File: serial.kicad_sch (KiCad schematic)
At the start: 28 parts, among them U12 6551, U13 4069, U14 LM348DR, X2 1.8432MHz

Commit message: fix OE timing on SRAM
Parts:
- renumbered D2 to D10, D2 to D11, D2 to D12, D2 to D13, D2 to D14, D2 to D15, D2 to D16, D2 to D17, R28 to R35, R28 to R37, R28 to R44, R28 to R53, R28 to R54, R28 to R55, R28 to R57, R28 to R58, R28 to R59, R28 to R60

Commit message: update page info
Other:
- company: (none) -> Dragon Data
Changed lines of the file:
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@@
 (kicad_sch (version 20230121) (generator eeschema)
-  (paper "A4")
+  (paper "A3")
+  (title_block
+    (date "2024-01-07")
+    (rev "3.0")
+    (company "Dragon Data")
+    (comment 1 "Modified by Julian Brown")
+    (comment 2 "SAMx4 by Ciaran Anscomb")
+  )
   (junction (at 226.06 24.13) (diameter 0) (color 0 0 0 0)
   )

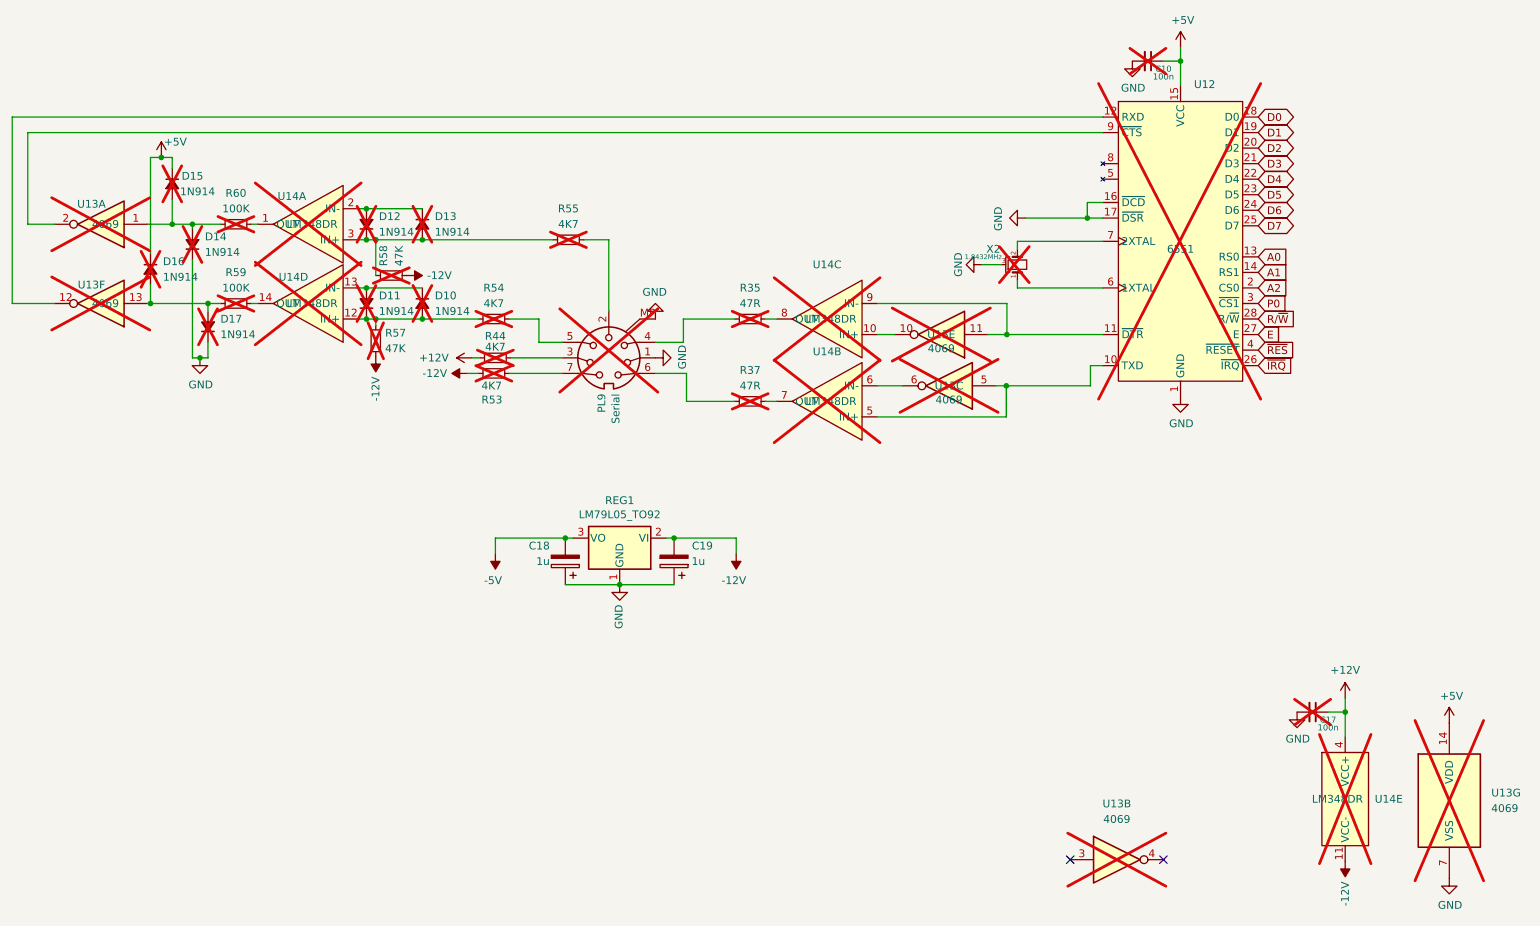
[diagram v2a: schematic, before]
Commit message: switch to fpga
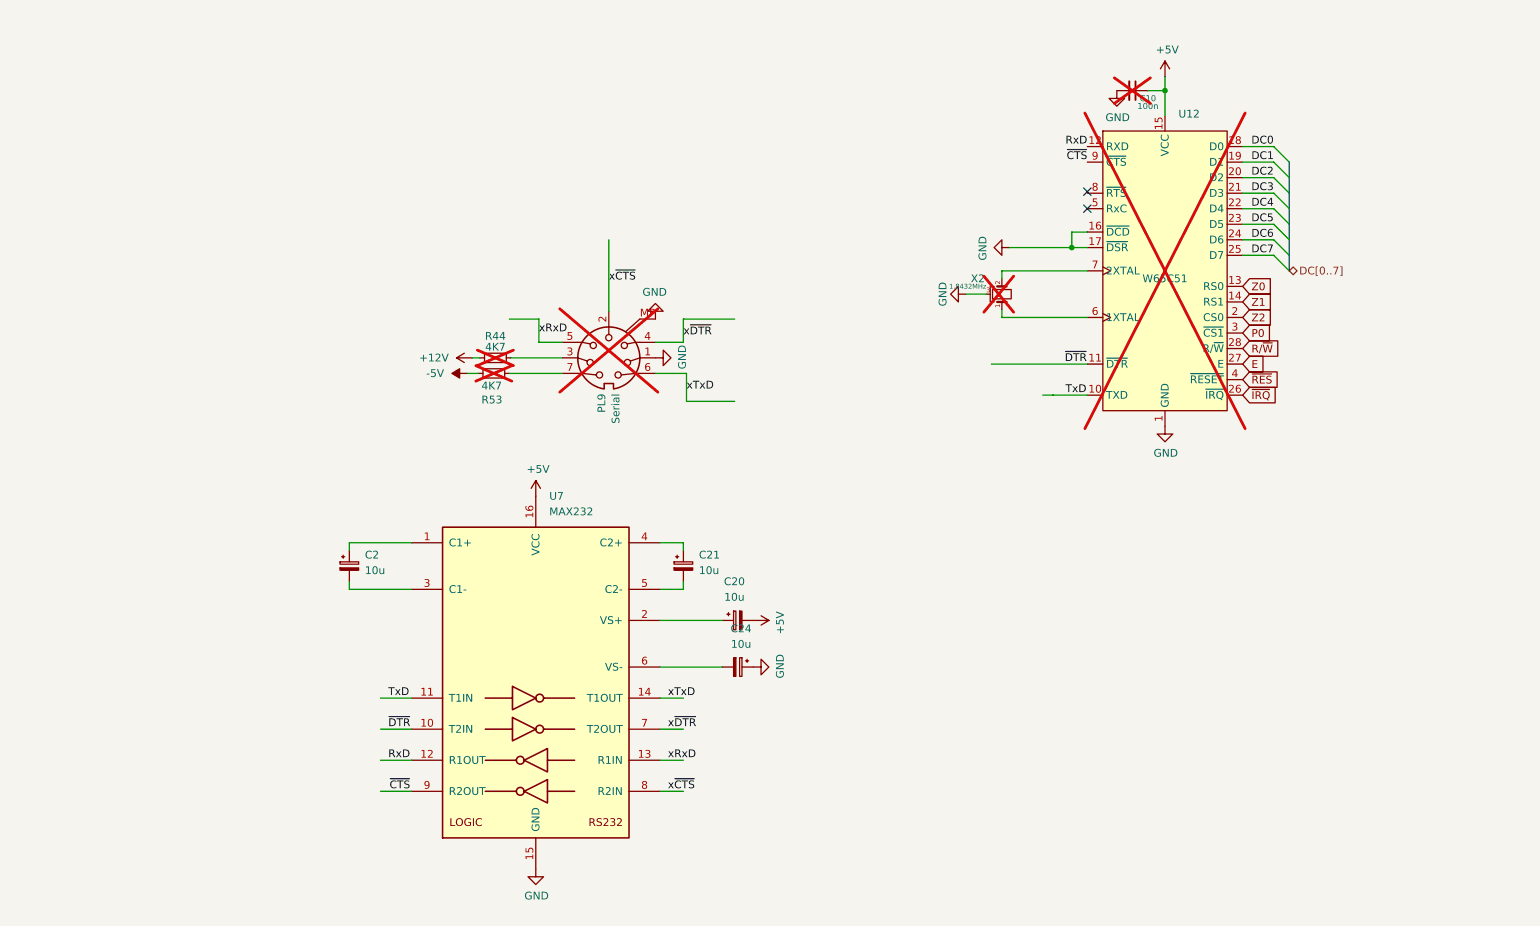
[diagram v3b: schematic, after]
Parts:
- removed C17: 100n, Capacitor_SMD:C_0805_2012Metric_Pad1.18x1.45mm_HandSolder, symbol Device:C_Small
- removed C18, C19: 1u, Capacitor_Tantalum_SMD:CP_EIA-3216-18_Kemet-A_Pad1.58x1.35mm_HandSolder, symbol Device:C_Polarized
- removed D10, D11, D12, D13, D14, D15, D16, D17: 1N914, Diode_SMD:D_SOD-323_HandSoldering, symbol Device:D_Small_Filled
- removed R35, R37: 47R, Resistor_SMD:R_0805_2012Metric_Pad1.20x1.40mm_HandSolder, symbol Device:R_Small
- removed R54, R55: 4K7, Resistor_SMD:R_0805_2012Metric_Pad1.20x1.40mm_HandSolder, symbol Device:R_Small
- removed R57, R58: 47K, Resistor_SMD:R_0805_2012Metric_Pad1.20x1.40mm_HandSolder, symbol Device:R_Small
- removed R59, R60: 100K, Resistor_SMD:R_0805_2012Metric_Pad1.20x1.40mm_HandSolder, symbol Device:R_Small
- removed REG1: LM79L05_TO92, Package_TO_SOT_SMD:SOT-89-3_Handsoldering, symbol Regulator_Linear:LM79L05_TO92
- removed U13: 4069, Package_SO:SOIC-14_3.9x8.7mm_P1.27mm, symbol 4xxx:4069
- removed U14: LM348DR, Package_SO:SOIC-14_3.9x8.7mm_P1.27mm, symbol Motorola PIA:LM348x
- added C2, C20, C21, C24: 10u, Capacitor_SMD:CP_Elec_5x5.3, symbol Device:C_Polarized_Small
- added U7: MAX232, Package_SO:SOIC-16_3.9x9.9mm_P1.27mm, symbol Interface_UART:MAX232
- U12: value 6551 -> W65C51; footprint Package_DIP:DIP-28_W15.24mm -> Package_LCC:PLCC-28_SMD-Socket
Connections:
- net -12V is gone; now on net -5V: R53.2
- net +5V: now also C20.2, U7.16 (VCC)
- net GND: now also C24.1, U7.15 (GND)
- net TxD: now reaches U12.10 (TXD)
- net TxD: now also U7.11 (T1IN)
- net xRxD: now reaches PL9.5
- net xRxD: now also U7.13 (R1IN)
- net ~{DTR}: now reaches U12.11 (~{DTR})
- net ~{DTR}: now also U7.10 (T2IN)
- net RxD: now reaches U12.12 (RXD)
- net RxD: now also U7.12 (R1OUT)
- net ~{CTS}: now reaches U12.9 (~{CTS})
- net ~{CTS}: now also U7.9 (R2OUT)
- net xTxD: now reaches PL9.6
- net xTxD: now also U7.14 (T1OUT)
- net x~{DTR}: now reaches PL9.4
- net x~{DTR}: now also U7.7 (T2OUT)
- net x~{CTS}: now reaches PL9.2
- net x~{CTS}: now also U7.8 (R2IN)
- net A0 renamed Z0
- net A1 renamed Z1
- net A2 renamed Z2
- net D0 renamed DC0
- net D1 renamed DC1
- net D2 renamed DC2
- net D3 renamed DC3
- net D4 renamed DC4
- net D5 renamed DC5
- net D6 renamed DC6
- net D7 renamed DC7
- new net: C20.1, U7.2 (VS+)
- new net: C2.1, U7.1 (C1+)
- new net: C2.2, U7.3 (C1-)
- new net: C21.1, U7.4 (C2+)
- new net: C21.2, U7.5 (C2-)
- new net: C24.2, U7.6 (VS-)
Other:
- moved on the sheet: C10, X2

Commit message: rework traces for FPGA
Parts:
- PL9: symbol dragon64:DIN-7-MP -> Connector:DIN-7
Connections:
- net GND: no longer PL9.MP
- net ~{IRQ} renamed ~{IRQx}
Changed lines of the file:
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@@
+		)
+	)
+	(global_label "~{IRQx}"
+		(shape input)
+		(at 236.22 78.74 0)
+		(fields_autoplaced yes)
+		(effects
+			(font
+				(size 1.27 1.27)
+			)
+			(justify left)
+		)
+		(property "Intersheetrefs" "${INTERSHEET_REFS}"
+			(at 242.7844 78.74 0)
+			(effects
+				(font
+					(size 1.27 1.27)
+				)
+				(justify left)
+				(hide yes)
+			)
 		)
 	)
@@
 		)
 	)
-	(global_label "~{IRQ}"
-		(shape input)
-		(at 236.22 78.74 0)
-		(fields_autoplaced yes)
-		(effects
-			(font
-				(size 1.27 1.27)
-			)
-			(justify left)
-		)
-		(property "Intersheetrefs" "${INTERSHEET_REFS}"
-			(at 241.7494 78.6606 0)
-			(effects
-				(font
-					(size 1.27 1.27)
-				)
-				(justify left)
-				(hide yes)
-			)
-		)
-	)
 	(global_label "~{RES}"
 		(shape input)
@@
 	)
 	(symbol
-		(lib_id "dragon64:DIN-7-MP")
+		(lib_id "Connector:DIN-7")
 		(at 132.588 72.644 0)
 		(mirror y)
@@
 			)
 		)
-		(property "Description" ""
+		(property "Description" "7-pin DIN connector"
 			(at 132.588 72.644 0)
 			(effects
@@
 		(pin "7"
 		)
-		(pin "MP"
-		)
-		(instances
+		(instances
